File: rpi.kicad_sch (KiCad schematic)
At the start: 35 parts, among them J1 Conn_02x08_Counter_Clockwise_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, J101 Conn_01x03_Pin, J4 Conn_01x04_Pin, J5 Conn_02x08_Counter_Clockwise_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, J6 2169890001, U3 RASPBERRY_PI_ZERO_2_W

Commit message: Pocetak PCB dizajna
Dodao fizicke definicije ploce
Dodao rupe za montazu
Kreirao inicijalnijalni placement
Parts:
- added H1, H2, H3, H4, H5: MountingHole_Pad, MountingHole:MountingHole_3.2mm_M3_DIN965_Pad_TopBottom, symbol Mechanical:MountingHole_Pad
- J1, J5: footprint Connector_Molex:Molex_Micro-Fit_3.0_43045-1621_2x08-1MP_P3.00mm_Horizontal -> Connector_FFC-FPC:Hirose_FH12-16S-0.5SH_1x16-1MP_P0.50mm_Horizontal
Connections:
- net +3V3: no longer J1.15 (Pin_15), J5.15 (Pin_15)
- net GND: now also H1.1, H2.1, H3.1, H4.1, H5.1
- new net +3.3V: J1.15 (Pin_15), J5.15 (Pin_15)

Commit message: Napajanje
David i njegova biblioteka su pravili probleme
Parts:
- added J7: 430450800, 430450800:MOLEX_430450800, symbol 430450800:430450800
- added TP1, TP10, TP11, TP12, TP13, TP14, TP15, TP16, TP17, TP18, TP19, TP2, TP20, TP21, TP22, TP23, TP24, TP25, TP26, TP27, TP28, TP29, TP3, TP30, TP31, TP32, TP33, TP4, TP5, TP6, TP7, TP8, TP9: TestPoint, TestPoint:TestPoint_Pad_D1.0mm, symbol Connector:TestPoint
- renumbered H5 to H1, H1 to H5
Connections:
- net +3.3V: now also J7.7, TP30.1
- net +5V: now also J7.5, TP31.1
- net GND: now also J7.1, J7.6, TP33.1
- net GSM_NETWORK_LED: now also TP23.1
- net I2C_SCL: now also TP16.1
- net I2C_SDA: now also TP15.1
- net LOC_GPS: now also TP24.1
- net LORA_RESET: now also TP21.1
- net LORA_TEST0: now also TP27.1
- net LORA_TEST1: now also TP26.1
- net PPS_GPS: now also TP25.1
- net PWRKEY: now also TP22.1
- net RPI_I2C_SCL: now also TP18.1
- net RPI_I2C_SDA: now also TP17.1
- net SD_CS: now also TP14.1
- net SD_DOBROTA: now also TP12.1
- net SD_MOSI: now also TP11.1
- net SD_SCK: now also TP13.1
- net SWCLK: now also TP28.1
- net SWDIO: now also TP29.1
- net UART1_RX: now also TP9.1
- net UART1_TX: now also TP10.1
- net UART2_RX: now also TP7.1
- net UART2_TX: now also TP8.1
- net UART3_RX: now also TP5.1
- net UART3_TX: now also TP6.1
- net UART4_RX: now also J7.2, TP3.1
- net UART4_TX: now also J7.3, TP4.1
- net UART5_RX: now also TP1.1
- net UART5_TX: now also TP2.1
- net USB_DN: now also TP20.1
- net USB_DP: now also TP19.1
- new net VCC: J7.4, TP32.1
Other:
- moved on the sheet: H1, H2, H3, H4, H5, JP1, JP2, U3

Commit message: Znacajne izmene seme
Dodao prikljucak za UV senzor
Dodao reset za GPS
Dodao ext_ant za GPS
Dodao 3D modele
Dodao testpoint-e
Sredio semu malo
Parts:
- added J8: ~, Connector_Coaxial:SMA_Amphenol_132134-16_Vertical, symbol Connector:Conn_Coaxial
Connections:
- net GND: now also J8.2 (Ext)
- new net UV: J8.1 (In)
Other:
- note added: "DEBUG"
- note added: "Mounting"
- note added: "Prikljucak za napajanje"
- note added: "UV senzor"
- moved on the sheet: H1, H2, H3, H4, H5, J7

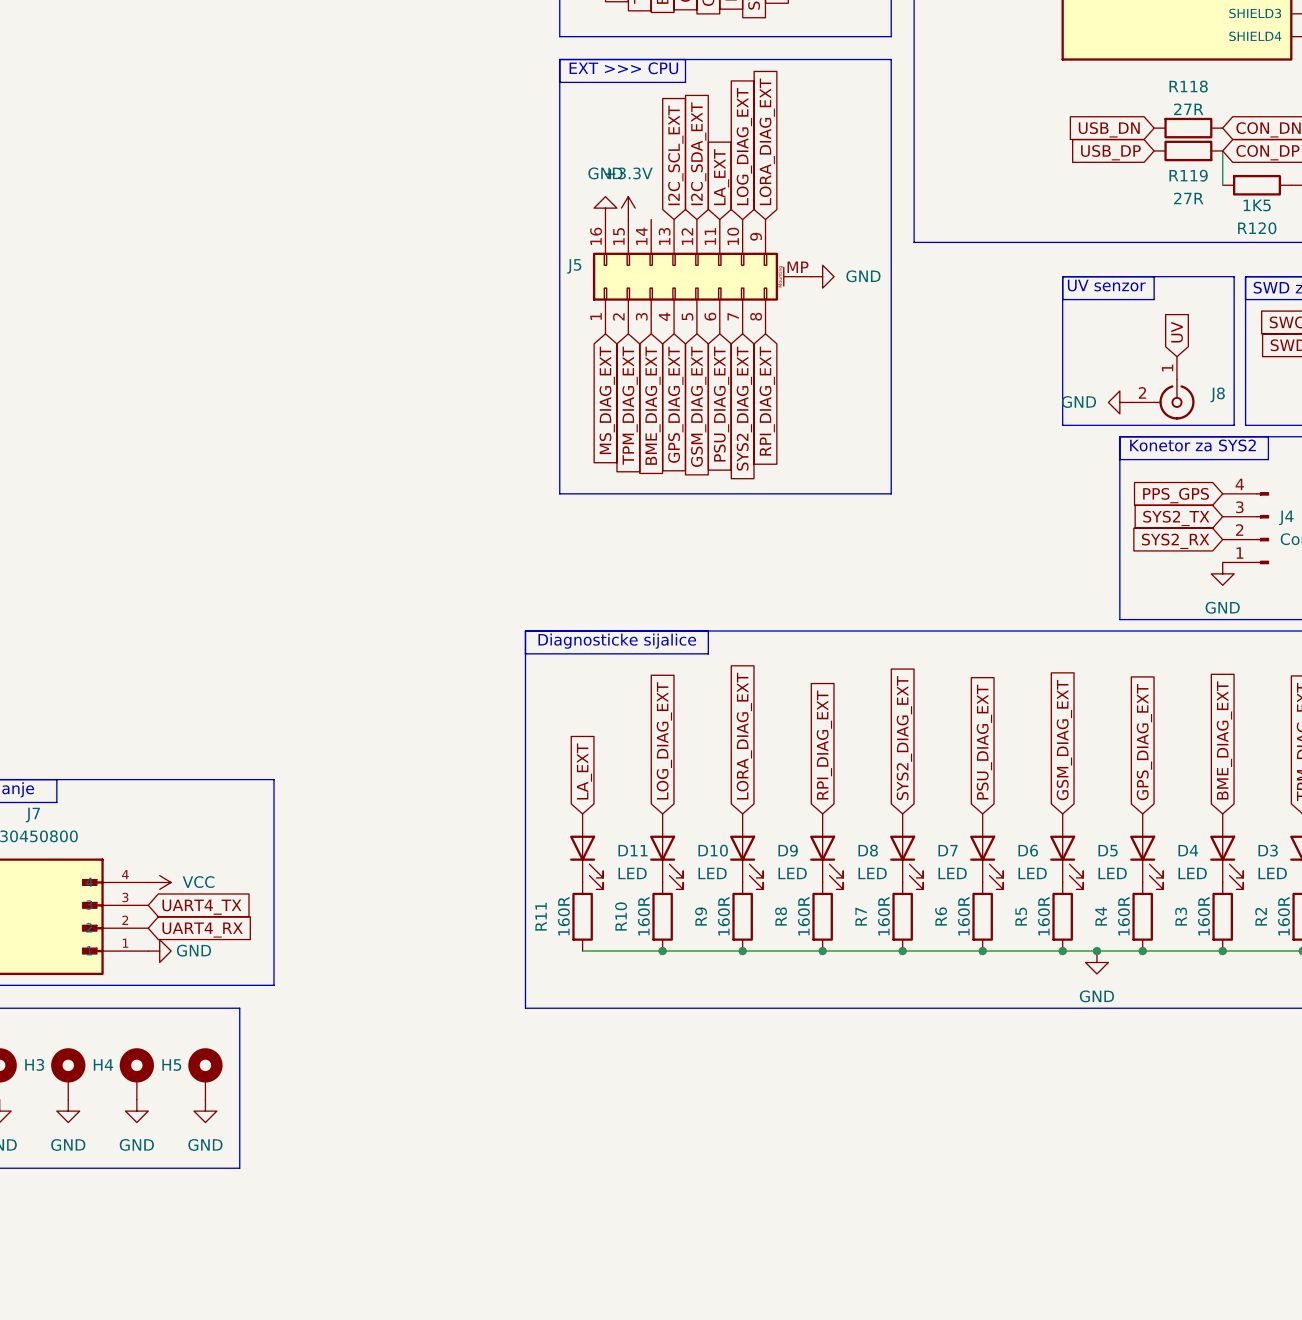
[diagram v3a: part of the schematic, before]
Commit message: Layout i rutiranje za EXT PCB uradjeni
Uradio sam layout i rutiranje za plocicu sa sijalicama i senzorom temperature koja ce biti montirana napolju
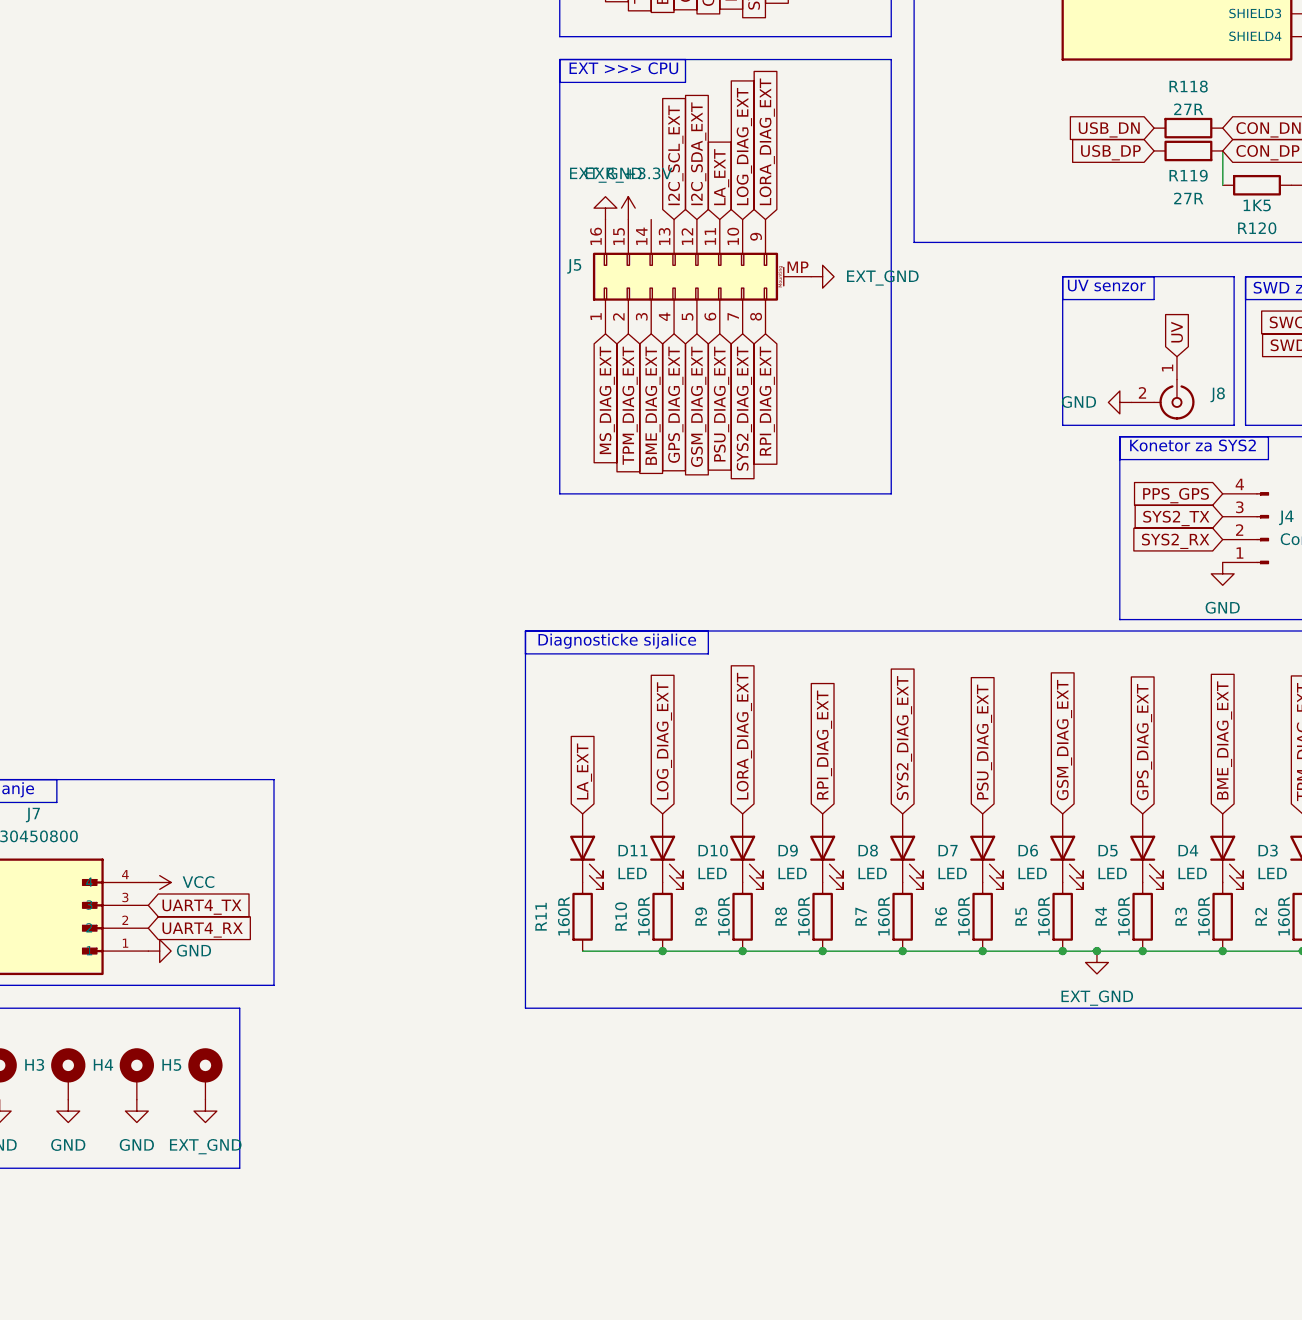
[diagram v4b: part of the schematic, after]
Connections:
- net +3.3V: no longer J5.15 (Pin_15)
- net GND: no longer H5.1, J5.16 (Pin_16), J5.MP (MountPin), R1.2, R10.2, R11.2, R2.2, R3.2, R4.2, R5.2, R6.2, R7.2, R8.2, R9.2
- new net EXR_+3.3V: J5.15 (Pin_15)
- new net EXT_GND: H5.1, J5.16 (Pin_16), J5.MP (MountPin), R1.2, R10.2, R11.2, R2.2, R3.2, R4.2, R5.2, R6.2, R7.2, R8.2, R9.2
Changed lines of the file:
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@@
 			)
 		)
-		(property "Value" "GND"
+		(property "Value" "EXT_GND"
 			(at 189.23 72.39 0)
 			(effects
@@
 	)
 	(symbol
-		(lib_id "power:GND")
-		(at 144.78 175.26 0)
-		(unit 1)
-		(exclude_from_sim no)
-		(in_bom yes)
-		(on_board yes)
-		(dnp no)
-		(fields_autoplaced yes)
-		(property "Reference" "#PWR071"
-			(at 144.78 181.61 0)
-			(effects
-				(font
-					(size 1.27 1.27)
-				)
-				(hide yes)
-			)
-		)
-		(property "Value" "GND"
-			(at 144.78 180.34 0)
-			(effects
-				(font
-					(size 1.27 1.27)
-				)
-			)
-		)
-		(property "Footprint" ""
-			(at 144.78 175.26 0)
-			(effects
-				(font
-					(size 1.27 1.27)
-				)
-				(hide yes)
-			)
-		)
-		(property "Datasheet" ""
-			(at 144.78 175.26 0)
-			(effects
-				(font
-					(size 1.27 1.27)
-				)
-				(hide yes)
-			)
-		)
-		(property "Description" "Power symbol creates a global label with name \"GND\" , ground"
-			(at 144.78 175.26 0)
-			(effects
-				(font
-					(size 1.27 1.27)
-				)
-				(hide yes)
-			)
-		)
-		(pin "1"
-		)
-		(instances
-			(project "SYS1"
-				(path "/38ef5478-8cbc-4f11-847b-fee2217190bd/84d9889a-c88c-49b5-af8d-2c98fb019d44"
-					(reference "#PWR071")
-					(unit 1)
-				)
-			)
-		)
-	)
-	(symbol
 		(lib_id "Jumper:SolderJumper_3_Open")
 		(at 29.21 67.31 180)
@@
 			)
 		)
-		(property "Value" "GND"
+		(property "Value" "EXT_GND"
 			(at 243.84 163.83 0)
 			(effects
@@
 			)
 		)
-		(property "Value" "+3.3V"
+		(property "Value" "EXR_+3.3V"
 			(at 191.77 72.39 0)
 			(effects
@@
 	)
 	(symbol
+		(lib_id "power:GND")
+		(at 212.09 83.82 90)
+		(unit 1)
+		(exclude_from_sim no)
+		(in_bom yes)
+		(on_board yes)
+		(dnp no)
+		(fields_autoplaced yes)
+		(property "Reference" "#PWR059"
+			(at 218.44 83.82 0)
+			(effects
+				(font
+					(size 1.27 1.27)
+				)
+				(hide yes)
+			)
+		)
+		(property "Value" "EXT_GND"
+			(at 215.9 83.8199 90)
+			(effects
+				(font
+					(size 1.27 1.27)
+				)
+				(justify right)
+			)
+		)
+		(property "Footprint" ""
+			(at 212.09 83.82 0)
+			(effects
+				(font
+					(size 1.27 1.27)
+				)
+				(hide yes)
+			)
+		)
+		(property "Datasheet" ""
+			(at 212.09 83.82 0)
+			(effects
+				(font
+					(size 1.27 1.27)
+				)
+				(hide yes)
+			)
+		)
+		(property "Description" "Power symbol creates a global label with name \"GND\" , ground"
+			(at 212.09 83.82 0)
+			(effects
+				(font
+					(size 1.27 1.27)
+				)
+				(hide yes)
+			)
+		)
+		(pin "1"
+		)
+		(instances
+			(project "SYS1"
+				(path "/38ef5478-8cbc-4f11-847b-fee2217190bd/84d9889a-c88c-49b5-af8d-2c98fb019d44"
+					(reference "#PWR059")
+					(unit 1)
+				)
+			)
+		)
+	)
+	(symbol
 		(lib_id "Mechanical:MountingHole_Pad")
 		(at 114.3 172.72 0)
@@
 	)
 	(symbol
+		(lib_id "power:GND")
+		(at 144.78 175.26 0)
+		(unit 1)
+		(exclude_from_sim no)
+		(in_bom yes)
+		(on_board yes)
+		(dnp no)
+		(fields_autoplaced yes)
+		(property "Reference" "#PWR070"
+			(at 144.78 181.61 0)
+			(effects
+				(font
+					(size 1.27 1.27)
+				)
+				(hide yes)
+			)
+		)
+		(property "Value" "EXT_GND"
+			(at 144.78 180.34 0)
+			(effects
+				(font
+					(size 1.27 1.27)
+				)
+			)
+		)
+		(property "Footprint" ""
+			(at 144.78 175.26 0)
+			(effects
+				(font
+					(size 1.27 1.27)
+				)
+				(hide yes)
+			)
+		)
+		(property "Datasheet" ""
+			(at 144.78 175.26 0)
+			(effects
+				(font
+					(size 1.27 1.27)
+				)
+				(hide yes)
+			)
+		)
+		(property "Description" "Power symbol creates a global label with name \"GND\" , ground"
+			(at 144.78 175.26 0)
+			(effects
+				(font
+					(size 1.27 1.27)
+				)
+				(hide yes)
+			)
+		)
+		(pin "1"
+		)
+		(instances
+			(project "SYS1"
+				(path "/38ef5478-8cbc-4f11-847b-fee2217190bd/84d9889a-c88c-49b5-af8d-2c98fb019d44"
+					(reference "#PWR070")
+					(unit 1)
+				)
+			)
+		)
+	)
+	(symbol
 		(lib_id "Device:R")
 		(at 261.62 73.66 270)
@@
 					(unit 1)
 				)
-			)
-		)
-	)
-	(symbol
-		(lib_id "power:GND")
-		(at 212.09 83.82 90)
-		(unit 1)
-		(exclude_from_sim no)
-		(in_bom yes)
-		(on_board yes)
-		(dnp no)
-		(fields_autoplaced yes)
-		(property "Reference" "#PWR070"
-			(at 218.44 83.82 0)
-			(effects
-				(font
-					(size 1.27 1.27)
-				)
-				(hide yes)
-			)
-		)
-		(property "Value" "GND"
-			(at 215.9 83.8199 90)
-			(effects
-				(font
-					(size 1.27 1.27)
-				)
-				(justify right)
-			)
-		)
-		(property "Footprint" ""
-			(at 212.09 83.82 0)
-			(effects
-				(font
-					(size 1.27 1.27)
-				)
-				(hide yes)
-			)
-		)
-		(property "Datasheet" ""
-			(at 212.09 83.82 0)
-			(effects
-				(font
-					(size 1.27 1.27)
-				)
-				(hide yes)
-			)
-		)
-		(property "Description" "Power symbol creates a global label with name \"GND\" , ground"
-			(at 212.09 83.82 0)
-			(effects
-				(font
-					(size 1.27 1.27)
-				)
-				(hide yes)
-			)
-		)
-		(pin "1"
-		)
-		(instances
-			(project "SYS1"
-				(path "/38ef5478-8cbc-4f11-847b-fee2217190bd/84d9889a-c88c-49b5-af8d-2c98fb019d44"
-					(reference "#PWR070")
-					(unit 1)
-				)

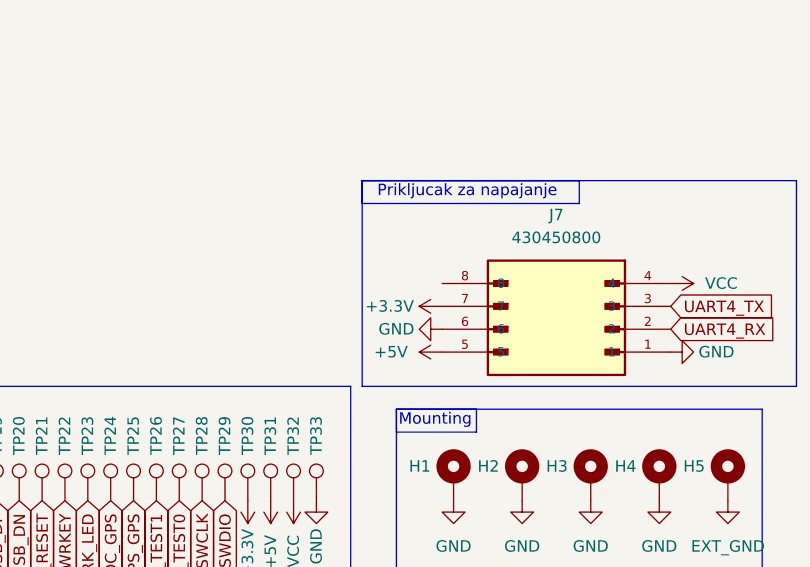
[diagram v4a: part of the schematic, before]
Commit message: Dodata baterija
Dodao pin za bateriju na konektor za napajanje
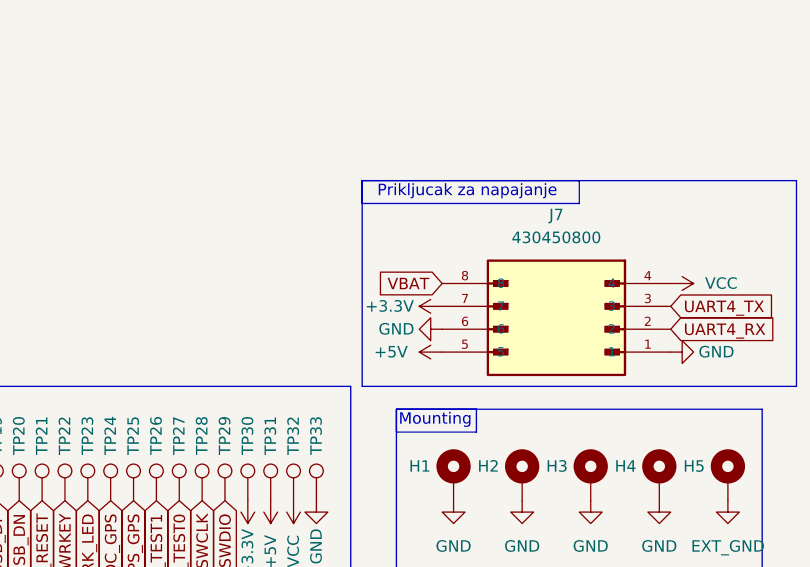
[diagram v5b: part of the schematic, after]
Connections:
- net VBAT: now reaches J7.8
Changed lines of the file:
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@@
+		)
+	)
+	(global_label "VBAT"
+		(shape input)
+		(at 113.03 151.13 180)
+		(fields_autoplaced yes)
+		(effects
+			(font
+				(size 1.27 1.27)
+			)
+			(justify right)
+		)
+		(property "Intersheetrefs" "${INTERSHEET_REFS}"
+			(at 105.63 151.13 0)
+			(effects
+				(font
+					(size 1.27 1.27)
+				)
+				(justify right)
+				(hide yes)
+			)
 		)
 	)

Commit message: Manje izmene seme
Sredio izgled seme
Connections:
- net EXR_+3.3V renamed EXT_+3.3V
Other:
- moved on the sheet: J5, J8
